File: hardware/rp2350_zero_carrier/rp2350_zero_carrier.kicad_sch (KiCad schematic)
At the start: 17 parts, among them J1 RP2350-Zero_Header(23pin,GPIO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, J2 USB-A_Host(Neltron_5075AR-04-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, J3 RP2350-Zero_Header(23pin,ボード2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, SW1 1回路2接点スイッチ(3pin,NKK_115643,ON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, SW2 1回路2接点スイッチ(3pin,NKK_115643,ON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, SW3 1回路2接点スイッチ(3pin,NKK_115643,ON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, SW4 1回路2接点スイッチ(3pin,NKK_115643,ON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, SW5 1回路2接点スイッチ(3pin,NKK_115643,ON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, SW6 タクトスイッチ4pin(Akizuki_DTS-63-N-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, U1 TPS2553DBVR

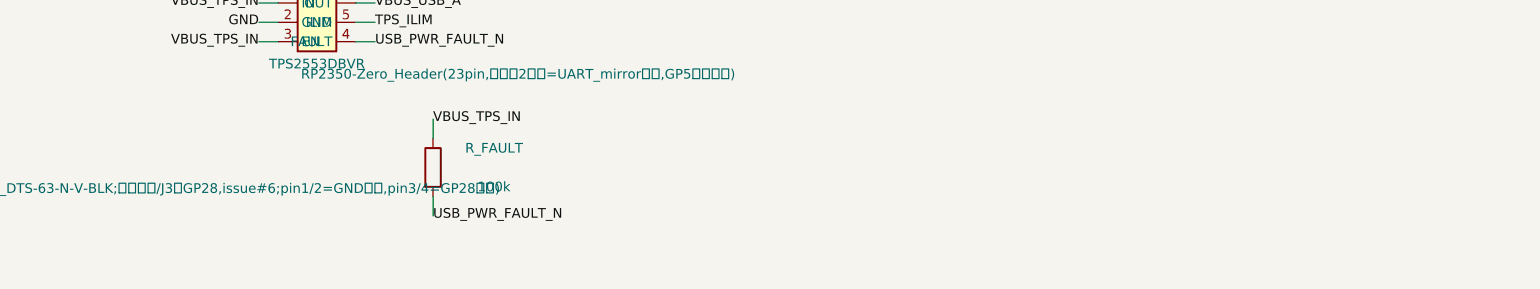
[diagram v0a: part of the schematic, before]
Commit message: fix(hardware): correct U1 (TPS2553DBVR) footprint vertical mirror
The custom TPS2553DBVR.kicad_mod placed pin1/pin3 (and pin4/pin6) with
the wrong Y sign, mirroring the whole SOT-23-6 pinout top-to-bottom
versus the datasheet (SLVS841F) and versus KiCad's own official
SOT-23-6 footprint (Package_TO_SOT_SMD.pretty, JEDEC MO-178), which
was used as an independent ground truth: it places pin1 at Y=-0.95
(top) and pin3 at Y=+0.95 (bottom), the opposite sign from ours.
Rendering both footprints to SVG confirmed the visual mirror directly.
Pad numbers/net assignments were already correct (per the earlier
tps-pinout-plan investigation) -- only the physical Y placement was
flipped, which is what the user spotted by eye in KiCad.

Fixed by negating pad 1/3/4/6 Y (pads 2/5 sit on Y=0, unaffected) and
the pin-1 silkscreen marker in both the library footprint and the
independently-embedded copy inside rp2350_zero_carrier.kicad_pcb
(placing an instance copies the footprint graphics into the board
file; a library edit alone does not update it).

Because EN/IN share a net, the pad flip is invisible to routing on
that side. FAULT and OUT (pad4/pad6) carry different nets and had
existing copper routed to their old (mirrored) positions, so the flip
alone shorted VBUS_USB_A to USB_PWR_FAULT_N and left both pads
unconnected. Rerouted both stubs locally: FAULT drops straight to
B.Cu at the pad (B.Cu is otherwise empty in this area) and rejoins
the original via-to-R_FAULT path; OUT's stub was re-routed around
pad5/R_ILIM and taps into the existing B.Cu trunk via a new via,
splitting it at the tap point. Refilled the GND_pour_bottom zone via
pcbnew's ZONE_FILLER (hand-edited copper doesn't trigger a refill, so
the stored fill polygon was stale and briefly reported a zone short
that a real fill resolves).

Also added the previously-planned (tps-pinout-plan, plan A) schematic
note by U1 documenting the EN/IN and OUT/net-name relationship, since
that's still a real readability issue independ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
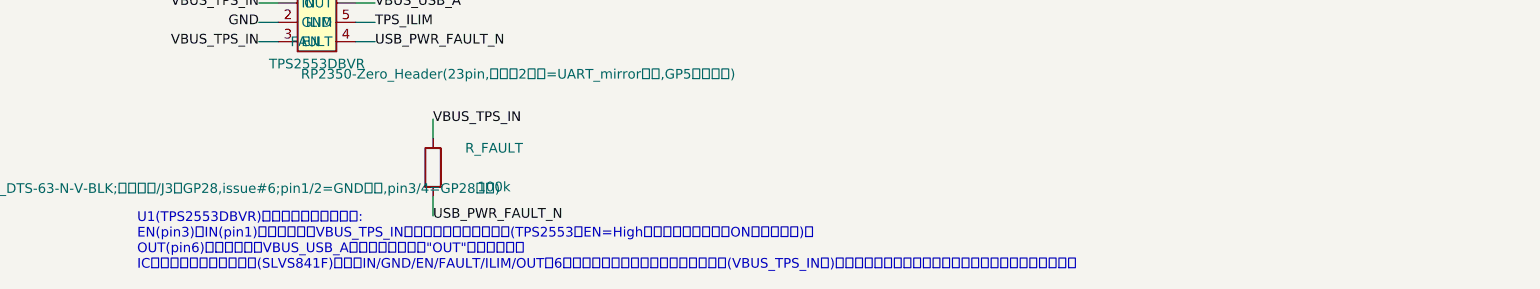
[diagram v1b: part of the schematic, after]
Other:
- note added: "U1(TPS2553DBVR)ピン配置に関する注記: EN(pin3)はIN(pin1)と同じネットVBUS_TPS_INに意図的に直結している(TPS2553はEN=Highでオンのため、常時ON固定の設計)。 OUT(pin6)のネット名はVBUS_USB_Aであり、文字列に"OUT"を含まない。 ICのピン名はデータシート(SLVS841F)準拠でIN/GND/EN/FAULT/ILIM/OUTの6本固定であり、ここに現れるネット名(VBUS_TPS_IN等)とは別物。照合はネット名ではなくピン名で行うこと。"
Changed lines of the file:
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@@
   (wire (pts (xy 243.84 226.06) (xy 243.84 228.6)) (stroke (width 0) (type default)) (uuid "b1c9a1a0-w011-4a00-9000-000000000001"))
   (label "USB_PWR_FAULT_N" (at 243.84 228.6 0) (effects (font (size 1.27 1.27)) (justify left)) (uuid "b1c9a1a0-l011-4a00-9000-000000000001"))
+  (text "U1(TPS2553DBVR)ピン配置に関する注記:\nEN(pin3)はIN(pin1)と同じネットVBUS_TPS_INに意図的に直結している(TPS2553はEN=Highでオンのため、常時ON固定の設計)。\nOUT(pin6)のネット名はVBUS_USB_Aであり、文字列に\"OUT\"を含まない。\nICのピン名はデータシート(SLVS841F)準拠でIN/GND/EN/FAULT/ILIM/OUTの6本固定であり、ここに現れるネット名(VBUS_TPS_IN等)とは別物。照合はネット名ではなくピン名で行うこと。"
+    (at 205 232 0)
+    (effects (font (size 1.27 1.27)) (justify left))
+    (uuid "b1c9a1a0-t001-4a00-9000-000000000001")
+  )
   (wire (pts (xy 243.84 218.44) (xy 243.84 215.9)) (stroke (width 0) (type default)) (uuid "b1c9a1a0-w012-4a00-9000-000000000001"))
   (label "VBUS_TPS_IN" (at 243.84 215.9 0) (effects (font (size 1.27 1.27)) (justify left)) (uuid "b1c9a1a0-l012-4a00-9000-000000000001"))
